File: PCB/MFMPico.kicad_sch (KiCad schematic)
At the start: 54 parts, among them J1 ECON34, J2 Conn_02x04_Odd_Even, J3 Micro_SD_Card_Det1, J4 Conn_01x16, J5 Conn_01x04, J6 Conn_01x02, J7 DNP, J8 PLACE, J9 Conn_01x04, P1 CON20, SW1 SW_Push, U1 74LVC1G02, U3 74LS33, U4 74LS33, U5 SN65HVD33DR, U6 74LS05, U7 SN74LVC1G00DBV, U8 SN74LVC1G00DBV

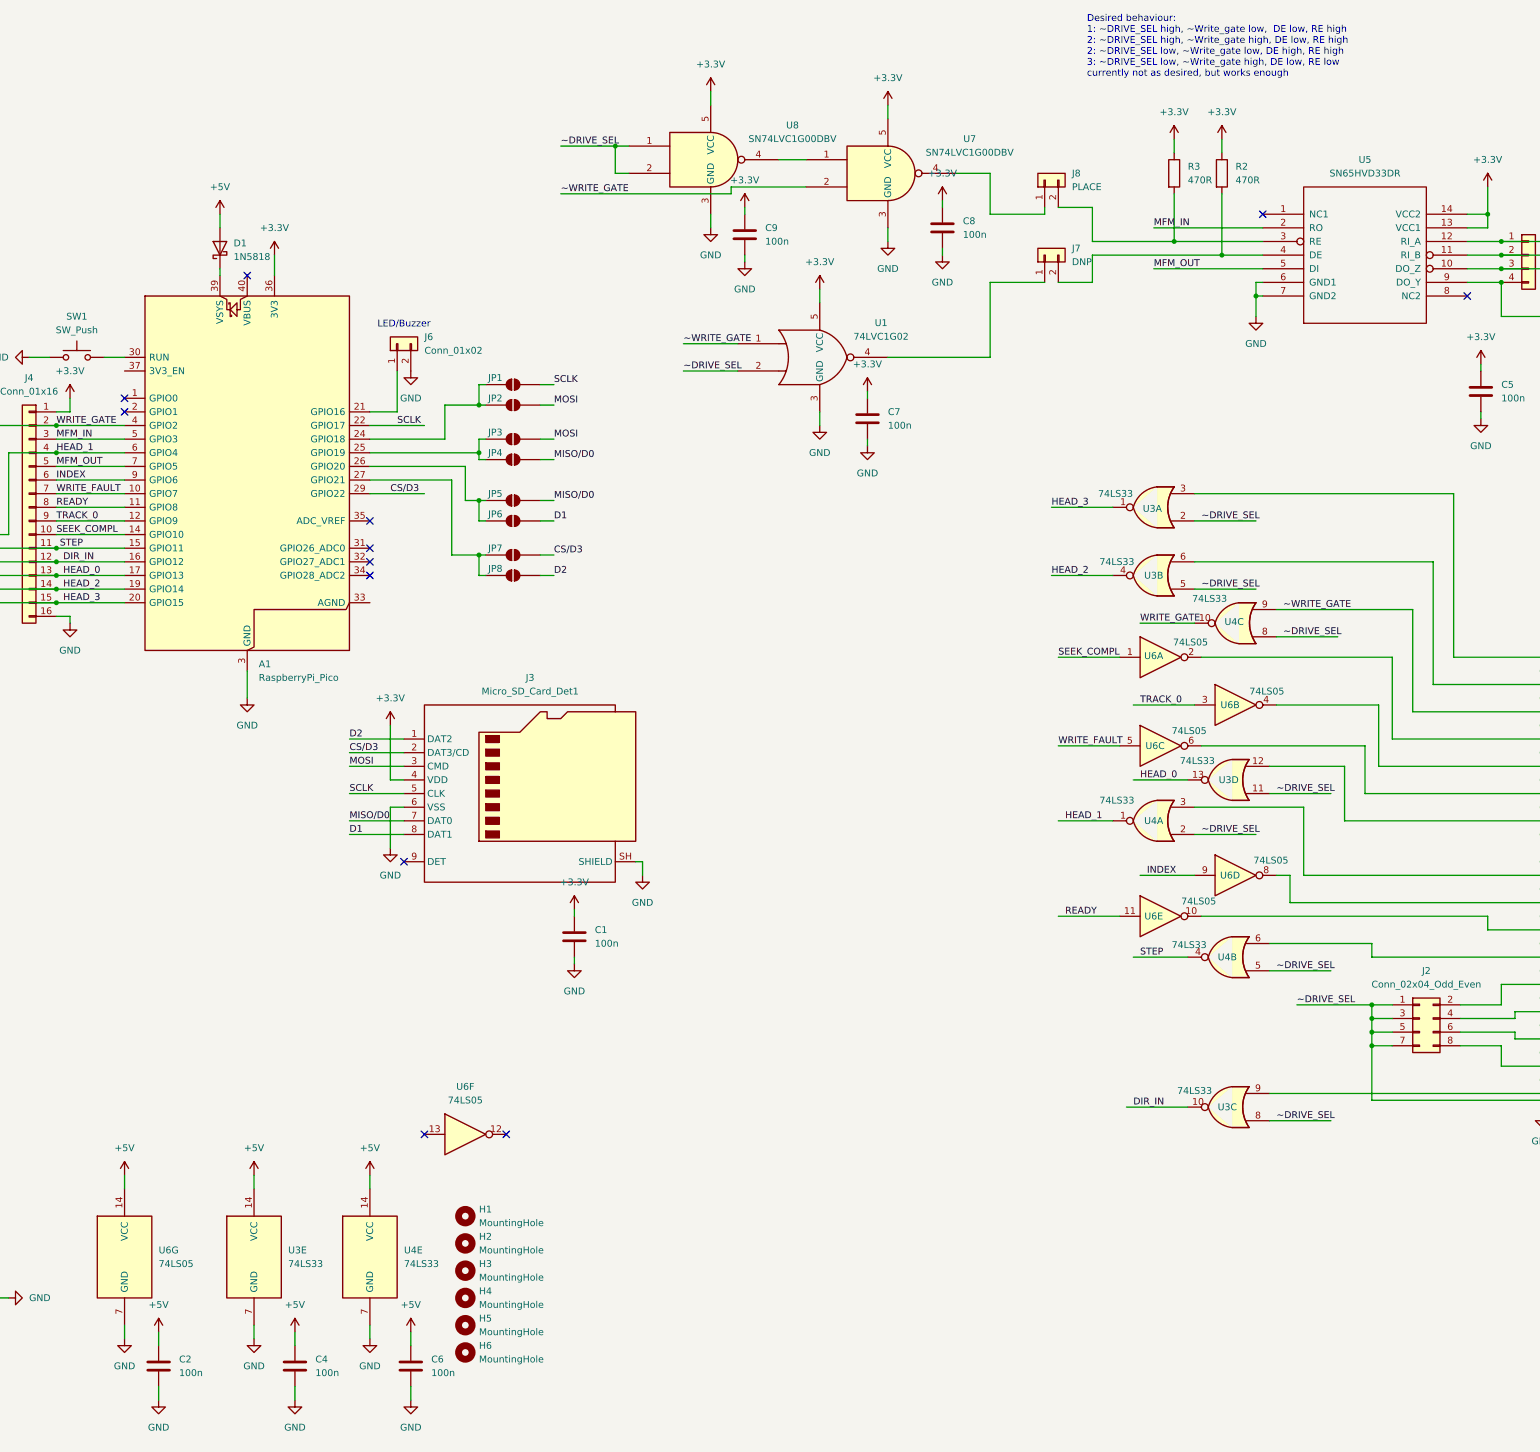
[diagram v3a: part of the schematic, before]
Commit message: New PCB works, apart from an odd low level format issue
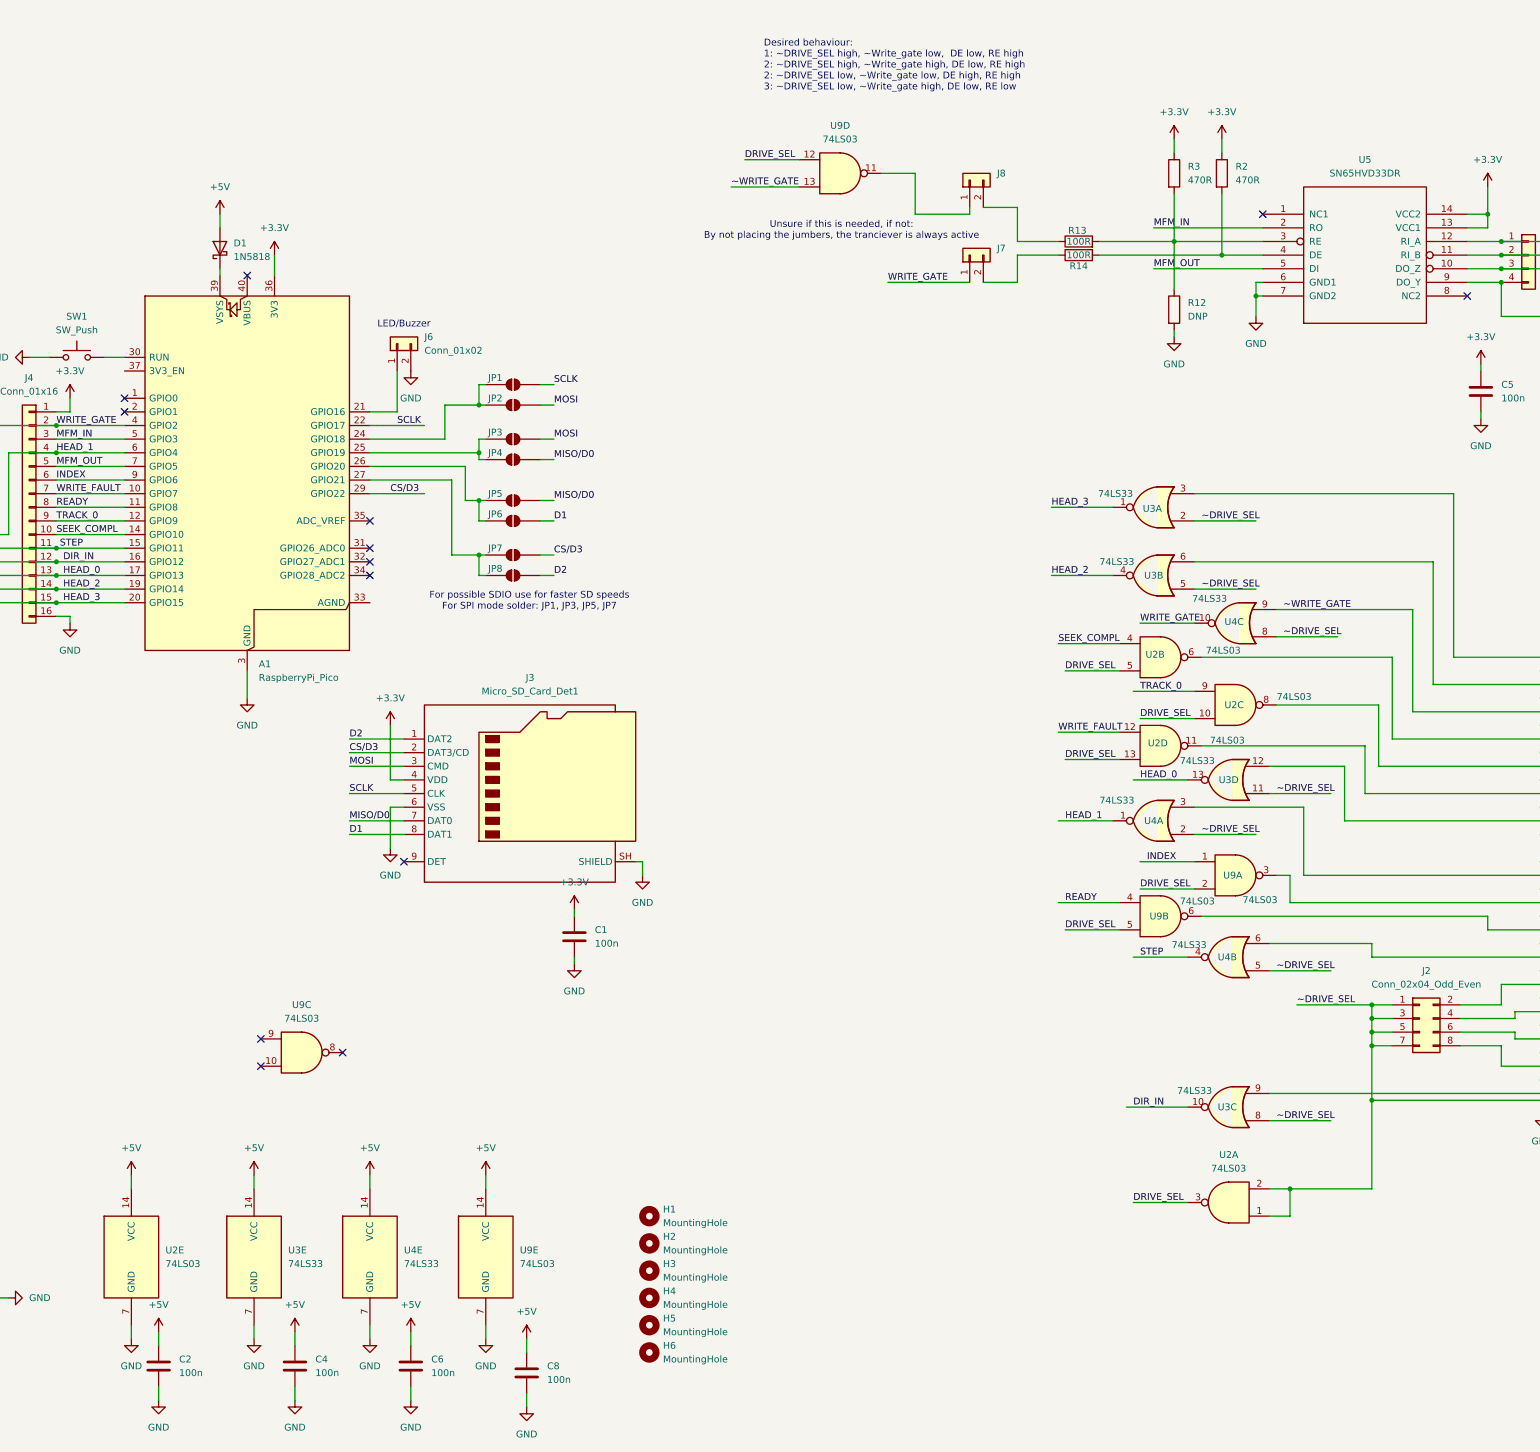
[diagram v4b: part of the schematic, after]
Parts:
- removed C7, C9: 100n, Capacitor_SMD:C_0603_1608Metric_Pad1.08x0.95mm_HandSolder, symbol Device:C
- removed U1: 74LVC1G02, Package_TO_SOT_SMD:SOT-23-5_HandSoldering, symbol 74xGxx:74LVC1G02
- removed U6: 74LS05, Package_DIP:DIP-14_W7.62mm, symbol 74xx:74LS05
- removed U7, U8: SN74LVC1G00DBV, Package_TO_SOT_SMD:SOT-23-5_HandSoldering, symbol 74xGxx:SN74LVC1G00DBV
- added R12: DNP, Resistor_SMD:R_0603_1608Metric, symbol Device:R
- added R13, R14: 100R, Resistor_SMD:R_0603_1608Metric, symbol Device:R
- added U2, U9: 74LS03, Package_DIP:DIP-14_W7.62mm, symbol 74xx:74LS03
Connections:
- net +3.3V: no longer C8.1
- net +5V: now also C8.1, U2.14 (VCC), U9.14 (VCC)
- net GND: now also R12.2, U2.7 (GND), U9.7 (GND)
- net INDEX: now also U9.1
- net READY: now also U9.4
- net SEEK_COMPL: now also U2.4
- net TRACK_0: now also U2.9
- net WRITE_FAULT: now also U2.12
- net WRITE_GATE: now also J7.1 (Pin_1)
- net ~DRIVE_SEL: now also U2.1, U2.2
- net ~WRITE_GATE: now also U9.13
- net at R2.2, U5.4 (DE): now also R14.2; no longer J7.2 (Pin_2)
- net at J8.1 (Pin_1): now also U9.11
- net at J1.8 (Seek_Complete): now also U2.6
- net at R3.2, U5.3 (RE): now also R12.1, R13.2; no longer J8.2 (Pin_2)
- net at J1.20 (Index): now also U9.3
- net at J1.10 (Track_0): now also U2.8
- net at J1.12 (Write_Fault): now also U2.11
- net at J1.22 (Ready): now also U9.6
- new net: J8.2 (Pin_2), R13.1
- new net: J7.2 (Pin_2), R14.1
- new net DRIVE_SEL: U2.10, U2.13, U2.3, U2.5, U9.12, U9.2, U9.5
- no-connect marks 19 -> 20
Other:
- note added: "Desired behaviour: 1: ~DRIVE_SEL high, ~Write_gate low, DE low, RE high 2: ~DRIVE_SEL high, ~Write_gate high, DE low, RE high 2: ~DRIVE_SEL low, ~Write_gate low, DE high, RE high 3: ~DRIVE_SEL low, ~Write_gate high, DE low, RE low"
- note added: "For possible SDIO use for faster SD speeds For SPI mode solder: JP1, JP3, JP5, JP7"
- note added: "Unsure if this is needed, if not: By not placing the jumbers, the tranciever is always active"
- note removed: "Desired behaviour: 1: ~DRIVE_SEL high, ~Write_gate low, DE low, RE high 2: ~DRIVE_SEL high, ~Write_gate high, DE low, RE high 2: ~DRIVE_SEL low, ~Write_gate low, DE high, RE high 3: ~DRIVE_SEL low, ~Write_gate high, DE low, RE low currently not as desired, but works enough"
- moved on the sheet: H1, H2, H3, H4, H5, H6, J7, J8
